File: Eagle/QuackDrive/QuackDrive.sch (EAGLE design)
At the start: 102 parts, among them IC1 MCP1703T-3302E/CB, IC10 TB67H450FNG,EL, IC12 TB67H450FNG,EL, IC2 MCP1703T-3302E/CB, IC4 TB67H450FNG,EL, IC6 TB67H450FNG,EL, IC8 TB67H450FNG,EL, Q1 NPN-BJT, Q2 NPN-BJT, U1 MPU-6050-1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

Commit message: new reference board desgn
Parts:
- removed C8, C9: 18pF, SparkFun:CAP0402
- added C18, C20: 18pF, SparkFun-Capacitors:18PF-0603-50V-5%
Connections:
- net GND: now also C18.1, C20.1; no longer C8.2, C9.2
- net OSC_IN: now also C20.2; no longer C9.1
- net OSC_OUT: now also C18.2; no longer C8.1
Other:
- moved on the sheet: SJ4
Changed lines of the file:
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@@
 <part name="C3" library="SparkFun2" deviceset="CAP" device="0805" value="10uF"/>
 <part name="SUPPLY29" library="supply2" deviceset="V+" device="" value="AV+"/>
-<part name="C9" library="SparkFun" deviceset="CAP" device="0402" value="18pF"/>
-<part name="C8" library="SparkFun" deviceset="CAP" device="0402" value="18pF"/>
 <part name="SUPPLY1" library="supply2" deviceset="AGND" device="" value="AV-"/>
 <part name="SUPPLY2" library="supply2" deviceset="AGND" device="" value="AV-"/>
@@
 <part name="PAD23" library="wirepad" library_urn="urn:adsk.eagle:library:412" deviceset="SMD2" device="" package3d_urn="urn:adsk.eagle:package:30839/1"/>
 <part name="U3" library="ACS70331EESATR-005B3" deviceset="ACS70331EESATR-005B3" device=""/>
+<part name="C18" library="SparkFun-Capacitors" library_urn="urn:adsk.eagle:library:510" deviceset="18PF" device="-0603-50V-5%" package3d_urn="urn:adsk.eagle:package:37414/1" value="18pF"/>
+<part name="C20" library="SparkFun-Capacitors" library_urn="urn:adsk.eagle:library:510" deviceset="18PF" device="-0603-50V-5%" package3d_urn="urn:adsk.eagle:package:37414/1" value="18pF"/>
 </parts>
 <sheets>
@@
 <attribute name="VALUE" x="280.67" y="101.6" size="1.778" layer="96"/>
 </instance>
-<instance part="C9" gate="G$1" x="69.85" y="71.12" smashed="yes" rot="MR90">
-<attribute name="NAME" x="72.771" y="72.644" size="1.778" layer="95" rot="MR90"/>
-<attribute name="VALUE" x="67.691" y="72.644" size="1.778" layer="96" rot="MR90"/>
-</instance>
-<instance part="C8" gate="G$1" x="69.85" y="86.36" smashed="yes" rot="MR90">
-<attribute name="NAME" x="72.771" y="87.884" size="1.778" layer="95" rot="MR90"/>
-<attribute name="VALUE" x="67.691" y="87.884" size="1.778" layer="96" rot="MR90"/>
-</instance>
 <instance part="SUPPLY1" gate="G$1" x="223.52" y="102.87" smashed="yes">
 <attribute name="VALUE" x="220.853" y="99.695" size="1.778" layer="96"/>
@@
 <attribute name="NAME" x="227.33" y="266.7" size="1.778" layer="95" rot="R180"/>
 </instance>
-<instance part="SJ4" gate="1" x="67.31" y="124.46" smashed="yes" rot="R180">
-<attribute name="NAME" x="69.85" y="121.92" size="1.778" layer="95" rot="R180"/>
+<instance part="SJ4" gate="1" x="71.12" y="124.46" smashed="yes" rot="R180">
+<attribute name="NAME" x="73.66" y="121.92" size="1.778" layer="95" rot="R180"/>
 </instance>
 <instance part="IC6" gate="G$1" x="-199.39" y="234.95" smashed="yes" rot="R180">
@@
 <attribute name="NAME" x="-78.74" y="142.748" size="1.778" layer="95" rot="R180"/>
 <attribute name="VALUE" x="-78.74" y="176.53" size="1.778" layer="96" rot="R180"/>
+</instance>
+<instance part="C18" gate="G$1" x="72.39" y="86.36" smashed="yes" rot="R90">
+<attribute name="NAME" x="69.469" y="87.884" size="1.778" layer="95" font="vector" rot="R90"/>
+<attribute name="VALUE" x="74.549" y="87.884" size="1.778" layer="96" font="vector" rot="R90"/>
+</instance>
+<instance part="C20" gate="G$1" x="72.39" y="71.12" smashed="yes" rot="R90">
+<attribute name="NAME" x="69.469" y="72.644" size="1.778" layer="95" font="vector" rot="R90"/>
+<attribute name="VALUE" x="74.549" y="72.644" size="1.778" layer="96" font="vector" rot="R90"/>
 </instance>
 </instances>
@@
 <junction x="82.55" y="71.12"/>
 <label x="90.17" y="71.12" size="1.778" layer="95"/>
-<pinref part="C9" gate="G$1" pin="1"/>
 <pinref part="OSC" gate="G$1" pin="2"/>
+<pinref part="C20" gate="G$1" pin="2"/>
 </segment>
 </net>
@@
 <junction x="82.55" y="86.36"/>
 <label x="87.63" y="86.36" size="1.778" layer="95"/>
-<pinref part="C8" gate="G$1" pin="1"/>
 <pinref part="OSC" gate="G$1" pin="1"/>
+<pinref part="C18" gate="G$1" pin="2"/>
 </segment>
 </net>
@@
 </segment>
 <segment>
-<wire x1="72.39" y1="124.46" x2="95.25" y2="124.46" width="0.1524" layer="91"/>
+<wire x1="76.2" y1="124.46" x2="95.25" y2="124.46" width="0.1524" layer="91"/>
 <wire x1="95.25" y1="124.46" x2="95.25" y2="127" width="0.1524" layer="91"/>
 <label x="80.01" y="124.46" size="1.778" layer="95"/>
@@
 <pinref part="SUPPLY4" gate="G$1" pin="DGND"/>
 <pinref part="SJ4" gate="1" pin="2"/>
-<wire x1="62.23" y1="124.46" x2="59.69" y2="124.46" width="0.1524" layer="91"/>
+<wire x1="66.04" y1="124.46" x2="59.69" y2="124.46" width="0.1524" layer="91"/>
 <wire x1="59.69" y1="124.46" x2="59.69" y2="111.76" width="0.1524" layer="91"/>
 </segment>
 <segment>
 <wire x1="67.31" y1="86.36" x2="64.77" y2="86.36" width="0.1524" layer="91"/>
-<pinref part="C8" gate="G$1" pin="2"/>
 <pinref part="SUPPLY7" gate="G$1" pin="DGND"/>
+<pinref part="C18" gate="G$1" pin="1"/>
 </segment>
 <segment>
 <wire x1="67.31" y1="71.12" x2="64.77" y2="71.12" width="0.1524" layer="91"/>
-<pinref part="C9" gate="G$1" pin="2"/>
 <pinref part="SUPPLY6" gate="G$1" pin="DGND"/>
-</segment>
-<segment>
+<pinref part="C20" gate="G$1" pin="1"/>
+</segment>
+<segment>

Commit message: Finished off missing bits
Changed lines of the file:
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@@
 <?xml version="1.0" encoding="utf-8"?>
 <!DOCTYPE eagle SYSTEM "eagle.dtd">
-<eagle version="9.2.2">
+<eagle version="9.5.1">
 <drawing>
 <settings>
@@
 <pinref part="SJ6" gate="1" pin="1"/>
 <wire x1="5.08" y1="158.75" x2="5.08" y2="157.48" width="0.1524" layer="91"/>
-<wire x1="5.08" y1="157.48" x2="-12.7" y2="157.48" width="0.1524" layer="91"/>
-<wire x1="-12.7" y1="157.48" x2="-13.97" y2="157.48" width="0.1524" layer="91"/>
-<wire x1="-12.7" y1="157.48" x2="-12.7" y2="165.1" width="0.1524" layer="91"/>
-<junction x="-12.7" y="157.48"/>
+<wire x1="5.08" y1="157.48" x2="-13.97" y2="157.48" width="0.1524" layer="91"/>
 <label x="-12.7" y="167.64" size="1.778" layer="95"/>
 <pinref part="U3" gate="G$1" pin="IP-"/>

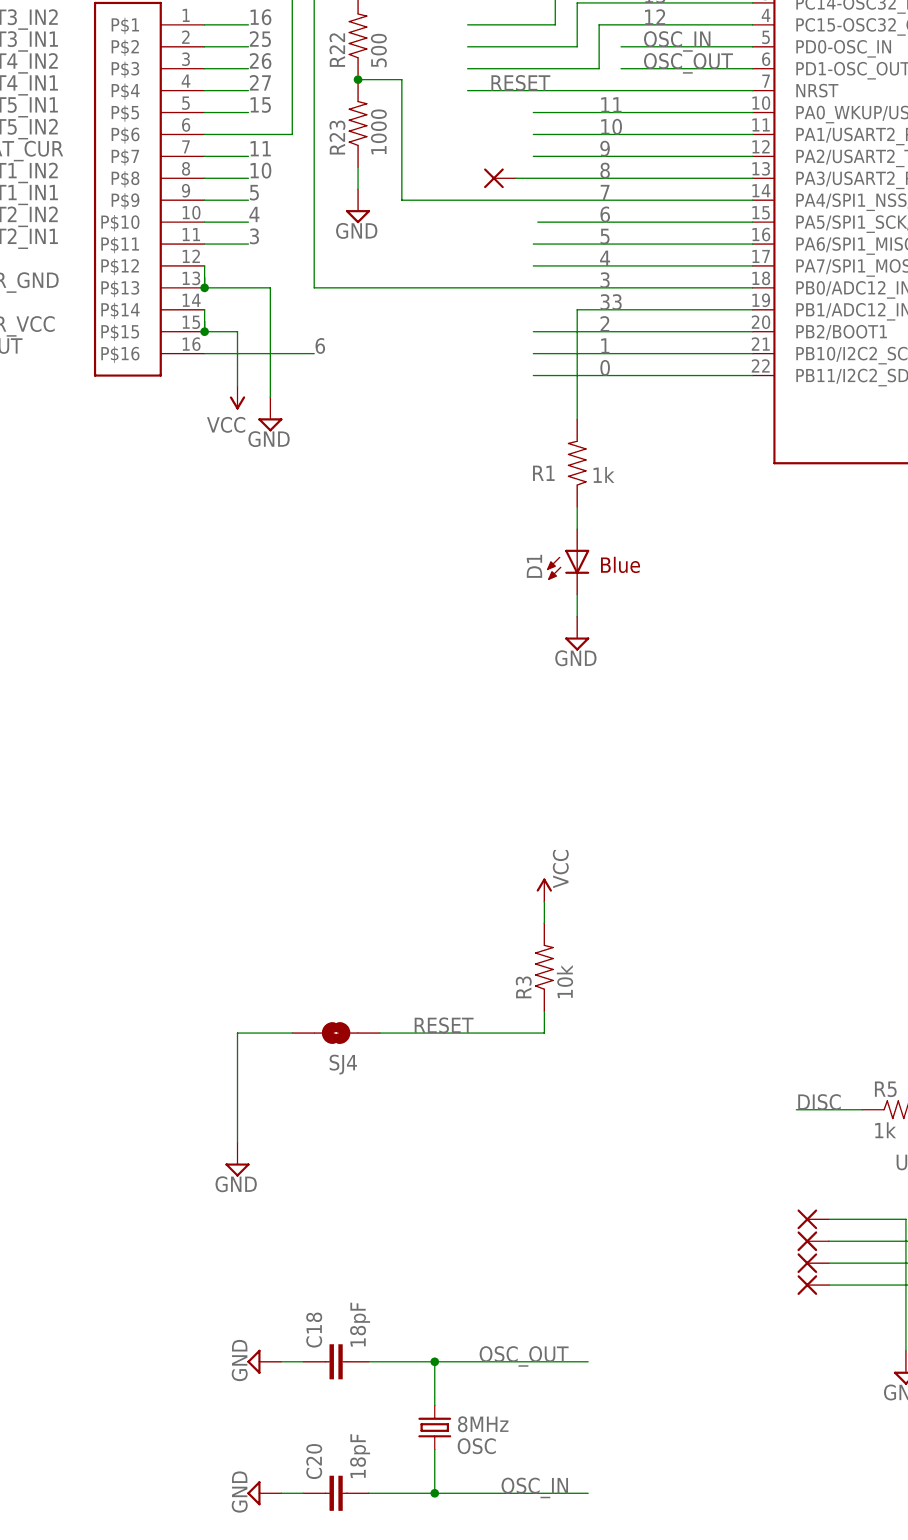
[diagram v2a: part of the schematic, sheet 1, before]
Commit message: Remove crystal, add Sbus inverter
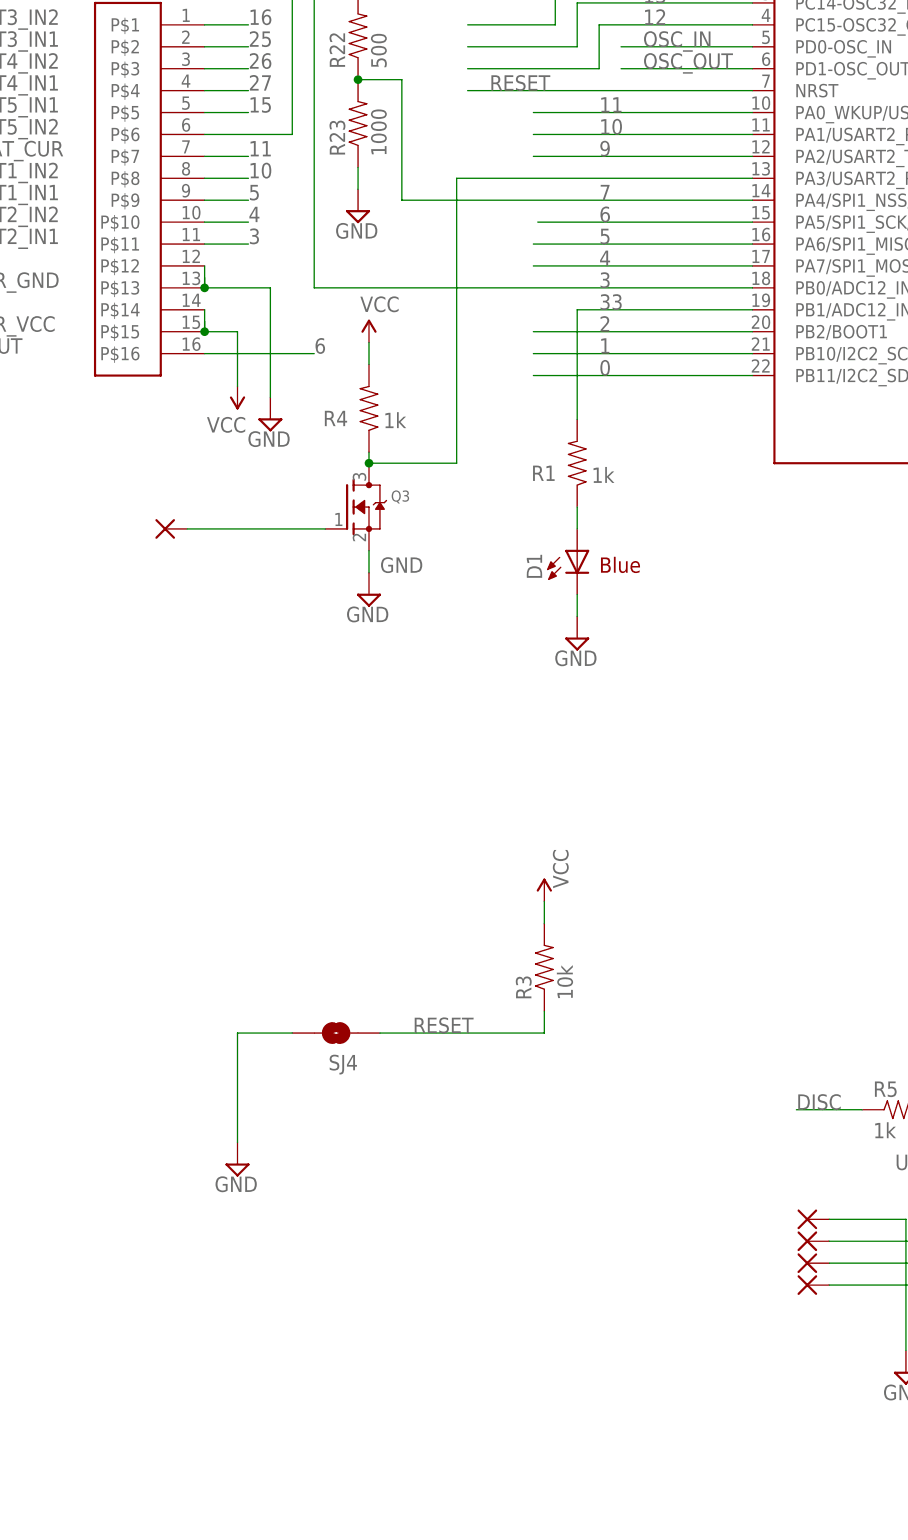
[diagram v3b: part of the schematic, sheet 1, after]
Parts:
- removed C18, C20: 18pF, SparkFun-Capacitors:18PF-0603-50V-5%
- removed OSC: 8MHz, SparkFun2:CRYSTAL5X3
- added Q3: (no value), adafruit:MOSFET-NREFLOW
- added R4: 1k, SparkFun:RESISTOR0402
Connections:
- removed net 8: PAD23.P, UC1.PA3/USART2_RX/ADC12_IN3/TIM2_CH4
- new net N$3: PAD23.P, Q3.G
- new net N$4: Q3.D, R4.1, UC1.PA3/USART2_RX/ADC12_IN3/TIM2_CH4
- net GND: now also Q3.S; no longer C18.1, C20.1
- net OSC_IN: no longer C20.2, OSC.2
- net OSC_OUT: no longer C18.2, OSC.1
- net VCC: now also R4.2
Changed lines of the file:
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@@
 <part name="SUPPLY3" library="supply2" deviceset="DGND" device="" value="GND"/>
 <part name="SUPPLY4" library="supply2" deviceset="DGND" device="" value="GND"/>
-<part name="SUPPLY6" library="supply2" deviceset="DGND" device="" value="GND"/>
-<part name="SUPPLY7" library="supply2" deviceset="DGND" device="" value="GND"/>
 <part name="SUPPLY10" library="supply2" deviceset="DGND" device="" value="GND"/>
 <part name="SUPPLY11" library="supply2" deviceset="DGND" device="" value="GND"/>
@@
 <part name="L1" library="SparkFun3" deviceset="INDUCTOR" device="0603" value="ferrite bead"/>
 <part name="SUPPLY17" library="supply2" deviceset="DGND" device="" value="GND"/>
-<part name="OSC" library="SparkFun2" deviceset="CRYSTAL" device="5X3" value="8MHz"/>
 <part name="VDD1" library="supply1" deviceset="VDD" device="" value="VIN"/>
 <part name="U1" library="Testing" deviceset="MPU-6050" device="-1"/>
@@
 <part name="PAD23" library="wirepad" library_urn="urn:adsk.eagle:library:412" deviceset="SMD2" device="" package3d_urn="urn:adsk.eagle:package:30839/1"/>
 <part name="U3" library="ACS70331EESATR-005B3" deviceset="ACS70331EESATR-005B3" device=""/>
-<part name="C18" library="SparkFun-Capacitors" library_urn="urn:adsk.eagle:library:510" deviceset="18PF" device="-0603-50V-5%" package3d_urn="urn:adsk.eagle:package:37414/1" value="18pF"/>
-<part name="C20" library="SparkFun-Capacitors" library_urn="urn:adsk.eagle:library:510" deviceset="18PF" device="-0603-50V-5%" package3d_urn="urn:adsk.eagle:package:37414/1" value="18pF"/>
+<part name="R4" library="SparkFun" deviceset="RESISTOR" device="0402" value="1k"/>
+<part name="SUPPLY6" library="supply2" deviceset="DGND" device="" value="GND"/>
+<part name="Q3" library="adafruit" deviceset="MOSFET-N" device="REFLOW"/>
+<part name="P+18" library="SparkFun" deviceset="VCC" device=""/>
 </parts>
 <sheets>
@@
 <attribute name="VALUE" x="57.023" y="106.045" size="1.778" layer="96"/>
 </instance>
-<instance part="SUPPLY6" gate="G$1" x="62.23" y="71.12" smashed="yes" rot="R270">
-<attribute name="VALUE" x="59.055" y="73.787" size="1.778" layer="96" rot="R270"/>
-</instance>
-<instance part="SUPPLY7" gate="G$1" x="62.23" y="86.36" smashed="yes" rot="R270">
-<attribute name="VALUE" x="59.055" y="89.027" size="1.778" layer="96" rot="R270"/>
-</instance>
 <instance part="SUPPLY10" gate="G$1" x="160.02" y="77.47" smashed="yes">
 <attribute name="VALUE" x="157.353" y="74.295" size="1.778" layer="96"/>
@@
 <instance part="SUPPLY17" gate="G$1" x="99.06" y="170.18" smashed="yes">
 <attribute name="VALUE" x="96.393" y="167.005" size="1.778" layer="96"/>
-</instance>
-<instance part="OSC" gate="G$1" x="82.55" y="78.74" smashed="yes" rot="MR270">
-<attribute name="NAME" x="85.09" y="77.47" size="1.778" layer="95" rot="MR180"/>
-<attribute name="VALUE" x="85.09" y="80.01" size="1.778" layer="96" rot="MR180"/>
 </instance>
 <instance part="VDD1" gate="G$1" x="223.52" y="133.35" smashed="yes">
@@
 <attribute name="VALUE" x="309.88" y="356.87" size="1.778" layer="96" rot="R270"/>
 </instance>
-<instance part="PAD23" gate="1" x="89.408" y="223.52" smashed="yes">
-<attribute name="VALUE" x="88.265" y="220.218" size="1.778" layer="96"/>
+<instance part="PAD23" gate="1" x="51.308" y="182.88" smashed="yes">
+<attribute name="VALUE" x="50.165" y="179.578" size="1.778" layer="96"/>
 </instance>
 <instance part="U3" gate="G$1" x="-31.75" y="158.75" smashed="yes" rot="R180">
@@
 <attribute name="VALUE" x="-78.74" y="176.53" size="1.778" layer="96" rot="R180"/>
 </instance>
-<instance part="C18" gate="G$1" x="72.39" y="86.36" smashed="yes" rot="R90">
-<attribute name="NAME" x="69.469" y="87.884" size="1.778" layer="95" font="vector" rot="R90"/>
-<attribute name="VALUE" x="74.549" y="87.884" size="1.778" layer="96" font="vector" rot="R90"/>
-</instance>
-<instance part="C20" gate="G$1" x="72.39" y="71.12" smashed="yes" rot="R90">
-<attribute name="NAME" x="69.469" y="72.644" size="1.778" layer="95" font="vector" rot="R90"/>
-<attribute name="VALUE" x="74.549" y="72.644" size="1.778" layer="96" font="vector" rot="R90"/>
+<instance part="R4" gate="G$1" x="74.93" y="196.85" smashed="yes" rot="MR90">
+<attribute name="NAME" x="69.596" y="194.7926" size="1.778" layer="95"/>
+<attribute name="VALUE" x="79.248" y="196.342" size="1.778" layer="96" rot="R180"/>
+</instance>
+<instance part="SUPPLY6" gate="G$1" x="74.93" y="175.26" smashed="yes">
+<attribute name="VALUE" x="72.263" y="172.085" size="1.778" layer="96"/>
+</instance>
+<instance part="Q3" gate="G$1" x="72.39" y="185.42" smashed="yes">
+<attribute name="NAME" x="77.47" y="186.055" size="1.27" layer="95"/>
+<attribute name="VALUE" x="77.47" y="184.15" size="1.27" layer="96"/>
+</instance>
+<instance part="P+18" gate="1" x="74.93" y="204.47" smashed="yes">
+<attribute name="VALUE" x="73.914" y="208.026" size="1.778" layer="96"/>
 </instance>
 </instances>
@@
 <wire x1="55.88" y1="208.28" x2="55.88" y2="205.74" width="0.1524" layer="91"/>
 </segment>
+<segment>
+<pinref part="P+18" gate="1" pin="VCC"/>
+<pinref part="R4" gate="G$1" pin="2"/>
+<wire x1="74.93" y1="204.47" x2="74.93" y2="201.93" width="0.1524" layer="91"/>
+</segment>
 </net>
 <net name="N$51" class="0">
@@
 <pinref part="UC1" gate="G$1" pin="PD0-OSC_IN"/>
 </segment>
-<segment>
-<wire x1="100.33" y1="71.12" x2="82.55" y2="71.12" width="0.1524" layer="91"/>
-<wire x1="82.55" y1="71.12" x2="74.93" y2="71.12" width="0.1524" layer="91"/>
-<wire x1="82.55" y1="76.2" x2="82.55" y2="71.12" width="0.1524" layer="91"/>
-<junction x="82.55" y="71.12"/>
-<label x="90.17" y="71.12" size="1.778" layer="95"/>
-<pinref part="OSC" gate="G$1" pin="2"/>
-<pinref part="C20" gate="G$1" pin="2"/>
-</segment>
 </net>
 <net name="OSC_OUT" class="0">
@@
 <label x="106.68" y="236.22" size="1.778" layer="95"/>
 <pinref part="UC1" gate="G$1" pin="PD1-OSC_OUT"/>
-</segment>
-<segment>
-<wire x1="100.33" y1="86.36" x2="82.55" y2="86.36" width="0.1524" layer="91"/>
-<wire x1="82.55" y1="86.36" x2="74.93" y2="86.36" width="0.1524" layer="91"/>
-<wire x1="82.55" y1="81.28" x2="82.55" y2="86.36" width="0.1524" layer="91"/>
-<junction x="82.55" y="86.36"/>
-<label x="87.63" y="86.36" size="1.778" layer="95"/>
-<pinref part="OSC" gate="G$1" pin="1"/>
-<pinref part="C18" gate="G$1" pin="2"/>
 </segment>
 </net>
@@
 </segment>
 <segment>
-<wire x1="67.31" y1="86.36" x2="64.77" y2="86.36" width="0.1524" layer="91"/>
-<pinref part="SUPPLY7" gate="G$1" pin="DGND"/>
-<pinref part="C18" gate="G$1" pin="1"/>
-</segment>
-<segment>
-<wire x1="67.31" y1="71.12" x2="64.77" y2="71.12" width="0.1524" layer="91"/>
-<pinref part="SUPPLY6" gate="G$1" pin="DGND"/>
-<pinref part="C20" gate="G$1" pin="1"/>
-</segment>
-<segment>
 <wire x1="160.02" y1="110.49" x2="160.02" y2="107.95" width="0.1524" layer="91"/>
 <pinref part="R11" gate="G$1" pin="1"/>
@@
 <wire x1="73.66" y1="222.25" x2="73.66" y2="224.79" width="0.1524" layer="91"/>
 <pinref part="SUPPLY9" gate="G$1" pin="DGND"/>
+</segment>
+<segment>
+<pinref part="Q3" gate="G$1" pin="S"/>
+<pinref part="SUPPLY6" gate="G$1" pin="DGND"/>
+<wire x1="74.93" y1="180.34" x2="74.93" y2="177.8" width="0.1524" layer="91"/>
+<label x="76.2" y="177.8" size="1.778" layer="95"/>
 </segment>
 </net>
@@
 </segment>
 </net>
-<net name="8" class="0">
-<segment>
+<net name="N$3" class="0">
+<segment>
+<pinref part="PAD23" gate="1" pin="P"/>
+<pinref part="Q3" gate="G$1" pin="G"/>
+<wire x1="53.848" y1="182.88" x2="69.85" y2="182.88" width="0.1524" layer="91"/>
+</segment>
+</net>
+<net name="N$4" class="0">
+<segment>
+<pinref part="R4" gate="G$1" pin="1"/>
+<pinref part="Q3" gate="G$1" pin="D"/>
+<wire x1="74.93" y1="191.77" x2="74.93" y2="190.5" width="0.1524" layer="91"/>
 <pinref part="UC1" gate="G$1" pin="PA3/USART2_RX/ADC12_IN3/TIM2_CH4"/>
-<pinref part="PAD23" gate="1" pin="P"/>
-<wire x1="119.38" y1="223.52" x2="91.948" y2="223.52" width="0.1524" layer="91"/>
-<label x="101.6" y="223.52" size="1.778" layer="95"/>
-</segment>
-</net>
+<wire x1="119.38" y1="223.52" x2="85.09" y2="223.52" width="0.1524" layer="91"/>
+<wire x1="85.09" y1="223.52" x2="85.09" y2="190.5" width="0.1524" layer="91"/>
+<wire x1="85.09" y1="190.5" x2="74.93" y2="190.5" width="0.1524" layer="91"/>
+<junction x="74.93" y="190.5"/>
+</segment>
+</net>
